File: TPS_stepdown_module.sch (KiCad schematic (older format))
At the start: 32 parts, among them J1 Vin, J2 Gnd, J3 Gnd, J4 Vout, U1 TPS54360DDA

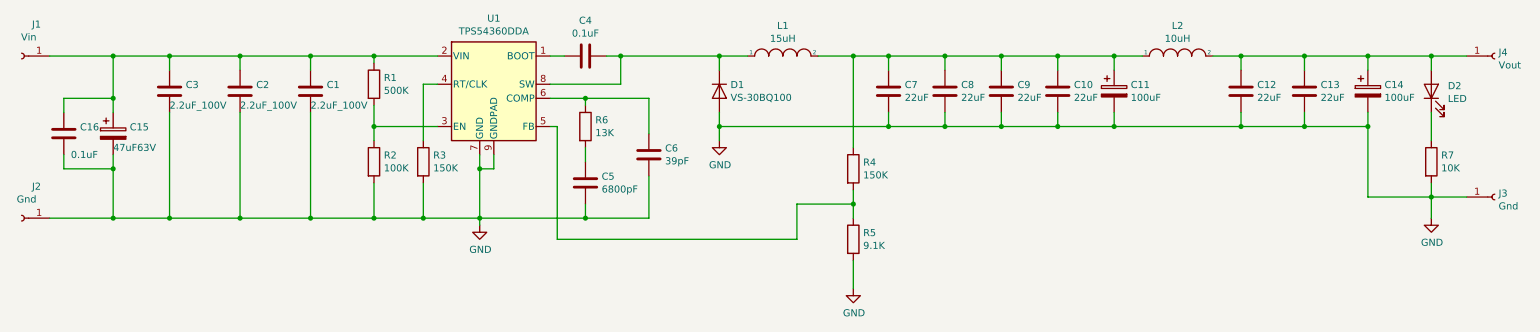
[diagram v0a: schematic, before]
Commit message: изменил размеры входной керамики
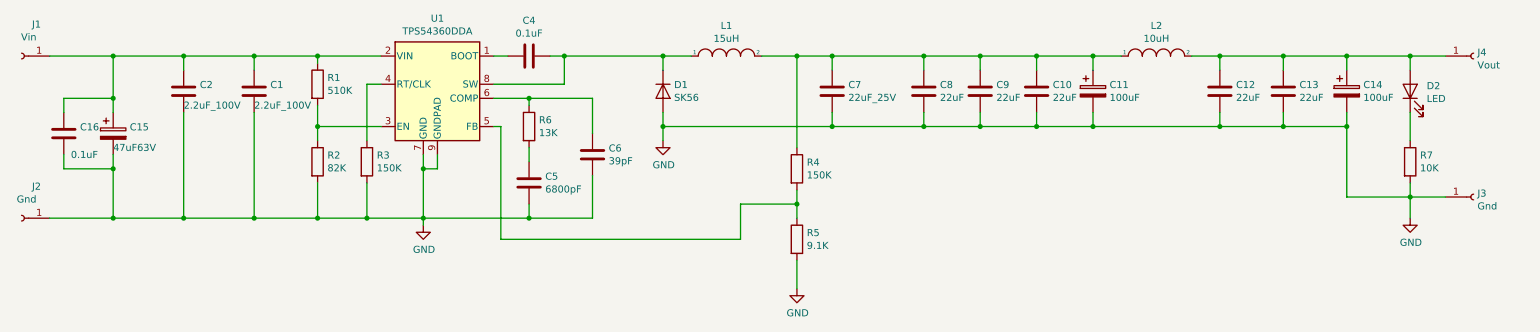
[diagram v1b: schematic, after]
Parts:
- removed C3: 2.2uF_100V, Capacitor_SMD:C_1206_3216Metric_Pad1.42x1.75mm_HandSolder, symbol Device:C
- C1, C2: footprint Capacitor_SMD:C_1206_3216Metric_Pad1.42x1.75mm_HandSolder -> Capacitor_SMD:C_1812_4532Metric_Pad1.30x3.40mm_HandSolder
- C7: value 22uF -> 22uF_25V
- D1: value VS-30BQ100 -> SK56; footprint Diode_SMD:D_SMC -> Diode_SMD:D_SMB
- R1: value 500K -> 510K
- R2: value 100K -> 82K
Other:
- moved on the sheet: C1, C10, C11, C12, C13, C14, C2, C4, C5, C6, C7, C8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
